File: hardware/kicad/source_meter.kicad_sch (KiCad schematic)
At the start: 39 parts, among them U501 TPS63020DSJ, U502 OPA365AIDBV, U503 LT3080EDD, U504 MCP4921-E/SN, U505 OPA197IDBV

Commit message: feat(hardware)!: draw draft A1 of the schematic around a Pico 2
A Raspberry Pi Pico 2 on two 1x20 sockets replaces the ESP32-S3
development board, the programmable logic device and the buffer
between the two boards (D-39 to D-43 of the specification). The former
interface and range logic sheets become two new ones:

- Controller: the Pico 2, the diodes that join its USB supply and the
  5 V rail of the carrier, resistor arrays in the SPI and acquisition
  lines, a reset button and a console header.
- Side Data: two shift registers that take the range, the status
  signals and the eight logic inputs with every sample.

The DUT connects through a 1x4 pin header and a lever terminal block
in parallel, both GND, VIN, VOUT, GND, and the logic port is a 1x10
header with VCC, GND, D7 to D0: the pin order of the PPK2 (D-44). A
solder jumper selects the supply of the DUT side of the level
translator. A transistor at the driver of the ampere switch holds it
open while VIN is above 5.5 V.

Reference designators are numbered as the annotation tool of KiCad
does by default (D-45). The numbering touches every sheet, so these
changes come in one commit. The symbol and the socket footprint of
the ESP32-S3 board leave the project library; the Pico 2 uses the
symbol and the footprint of the KiCad library.

The electrical rules check reports no errors and no warnings. The
parts stay candidates, and no program for the PIO blocks exists yet.

BREAKING CHANGE: the pins of the controller follow the new pin map of
section 5 of the specification.
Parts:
- R15: renamed from R501; value 470R -> 1k
- renumbered C501 to C24, C513 to C25, C502 to C26, C514 to C27, C503 to C28, C516 to C29, C517 to C30, C507 to C31, C504 to C32, C515 to C33, C505 to C34, C506 to C35, C508 to C36, C509 to C37, C510 to C38, C511 to C39, C512 to C40, FB501 to FB1, L501 to L2, R510 to R16, R511 to R17, R506 to R18, R512 to R19, R502 to R20, R505 to R21, R503 to R22, R504 to R23, R507 to R24, R508 to R25, R509 to R26, TP501 to TP11, TP503 to TP12, TP502 to TP13, U502 to U10, U505 to U11, U503 to U12, U504 to U8, U501 to U9
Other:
- note added: "V_PRE follows the set-point: PRE_FB = 0.2 x (V_PRE - SET_DRV) + 0.41 V and U9 holds it at 0.5 V, so V_PRE = SET_DRV + 0.45 V to 0.49 V (1.26 V at 0.8 V, 5.49 V at 5.0 V). SET_DRV = 2.1 x DAC: 0 V to 5.25 V in 1.28 mV steps. Firmware keeps it between 0.75 V and 5.0 V. U12: IN from V_PRE, VCONTROL from +13V5, minimum load R26 to -4V_A. U9 runs in forced PWM (PS/SYNC high), 2.4 MHz."
- note removed: "V_PRE follows the set-point: PRE_FB = 0.2 x (V_PRE - SET_DRV) + 0.41 V and U501 holds it at 0.5 V, so V_PRE = SET_DRV + 0.45 V to 0.49 V (1.26 V at 0.8 V, 5.49 V at 5.0 V). SET_DRV = 2.1 x DAC: 0 V to 5.25 V in 1.28 mV steps. Firmware keeps it between 0.75 V and 5.0 V. U503: IN from V_PRE, VCONTROL from +13V5, minimum load R509 to -4V_A. U501 runs in forced PWM (PS/SYNC high), 2.4 MHz."

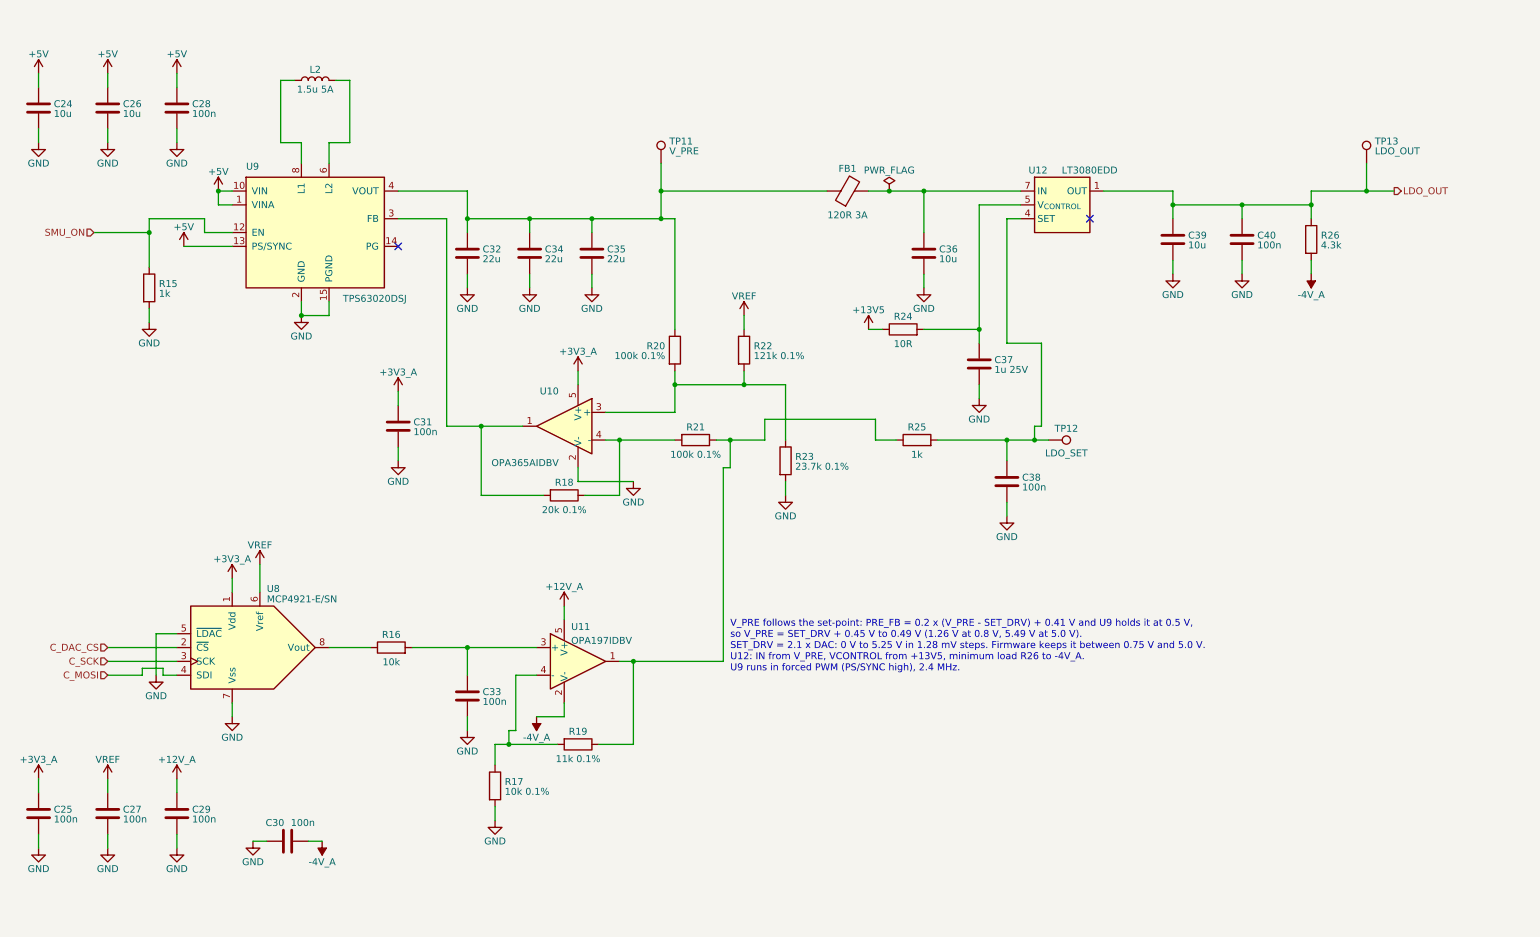
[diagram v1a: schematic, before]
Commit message: feat(hardware): draw draft A2 of the schematic
428 parts on 15 A4 pages, 14 sheets below the root sheet (D-83). Two
sheets are new: Logic Supplies, with the supervisor of the 5 V rail and
the two 3.3 V regulators, and Rail Monitor, with the comparators behind
PWR_GOOD.

The drawings follow the specification of draft A2: a current limiter
on each supply input and a priority multiplexer, a pre-regulator that
tracks the output of the linear regulator, a VIN path that withstands
-20 V to +20 V with its switch open, two diode-connected MOSFETs as
ladder clamp, thin-film and four-terminal shunts, ESD arrays at the CC
pins and at the VCC pin of the logic port. The reference designators
are numbered as KiCad numbers them (D-45), so they are not those of
draft A1.

The project library gains the symbol of the input multiplexer and two
footprints: the lever terminal block with pads of 1.9 mm x 2.3 mm and
the controller module without its antenna keep-out (D-85).

The electrical rules check reports no errors and no warnings. The
parts are candidates, and nothing is built or measured.
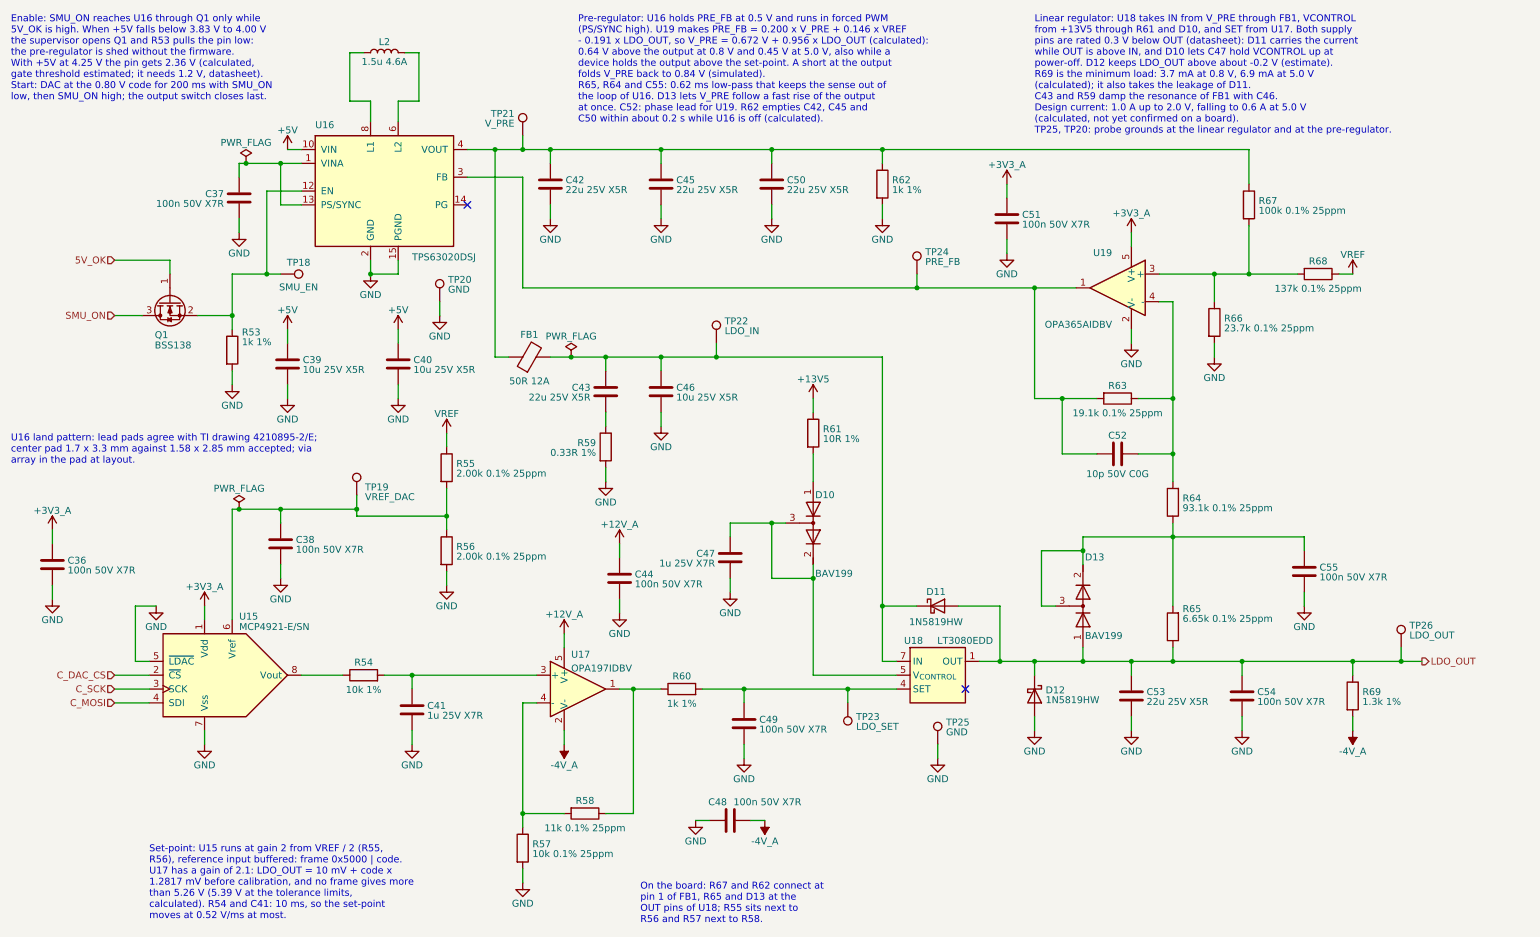
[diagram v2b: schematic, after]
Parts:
- added C43: 22u 25V X5R, Capacitor_SMD:C_1206_3216Metric, symbol Device:C
- added C52: 10p 50V C0G, Capacitor_SMD:C_0603_1608Metric, symbol Device:C
- added C55: 100n 50V X7R, Capacitor_SMD:C_0603_1608Metric, symbol Device:C
- added D10, D13: BAV199, Package_TO_SOT_SMD:SOT-23, symbol Device:D_Dual_Series_AKC
- added D11, D12: 1N5819HW, Diode_SMD:D_SOD-123, symbol Device:D_Schottky
- added Q1: BSS138, Package_TO_SOT_SMD:SOT-23, symbol Transistor_FET:BSS138
- added R55, R56: 2.00k 0.1% 25ppm, Resistor_SMD:R_0603_1608Metric, symbol Device:R
- added R59: 0.33R 1%, Resistor_SMD:R_0805_2012Metric, symbol Device:R
- added R62: 1k 1%, Resistor_SMD:R_0603_1608Metric, symbol Device:R
- added R65: 6.65k 0.1% 25ppm, Resistor_SMD:R_0603_1608Metric, symbol Device:R
- added TP18: SMU_EN, TestPoint:TestPoint_Pad_D1.5mm, symbol Connector:TestPoint
- added TP19: VREF_DAC, TestPoint:TestPoint_Pad_D1.5mm, symbol Connector:TestPoint
- added TP20, TP25: GND, TestPoint:TestPoint_Pad_2.0x2.0mm, symbol Connector:TestPoint
- added TP22: LDO_IN, TestPoint:TestPoint_Pad_D1.5mm, symbol Connector:TestPoint
- added TP24: PRE_FB, TestPoint:TestPoint_Pad_D1.5mm, symbol Connector:TestPoint
- C36: renamed from C25; value 100n -> 100n 50V X7R; MPN (none) -> C0603C104K5RACTU; Manufacturer (none) -> KEMET
- C37: renamed from C28; value 100n -> 100n 50V X7R; MPN (none) -> C0603C104K5RACTU; Manufacturer (none) -> KEMET
- C38: renamed from C27; value 100n -> 100n 50V X7R; MPN (none) -> C0603C104K5RACTU; Manufacturer (none) -> KEMET
- C39: renamed from C24; value 10u -> 10u 25V X5R; MPN (none) -> CL21A106KAYNNNE; Manufacturer (none) -> Samsung Electro-Mechanics
- C40: renamed from C26; value 10u -> 10u 25V X5R; MPN (none) -> CL21A106KAYNNNE; Manufacturer (none) -> Samsung Electro-Mechanics
- C41: renamed from C33; value 100n -> 1u 25V X7R; MPN (none) -> C0603C105K3RACTU; Manufacturer (none) -> KEMET
- C42: renamed from C32; value 22u -> 22u 25V X5R; footprint Capacitor_SMD:C_0805_2012Metric -> Capacitor_SMD:C_1206_3216Metric; MPN (none) -> CL31A226KAHNNNE; Manufacturer (none) -> Samsung Electro-Mechanics
- C44: renamed from C29; value 100n -> 100n 50V X7R; MPN (none) -> C0603C104K5RACTU; Manufacturer (none) -> KEMET
- C45: renamed from C34; value 22u -> 22u 25V X5R; footprint Capacitor_SMD:C_0805_2012Metric -> Capacitor_SMD:C_1206_3216Metric; MPN (none) -> CL31A226KAHNNNE; Manufacturer (none) -> Samsung Electro-Mechanics
- C46: renamed from C36; value 10u -> 10u 25V X5R; MPN (none) -> CL21A106KAYNNNE; Manufacturer (none) -> Samsung Electro-Mechanics
- C47: renamed from C37; value 1u 25V -> 1u 25V X7R; MPN (none) -> C0603C105K3RACTU; Manufacturer (none) -> KEMET
- C48: renamed from C30; value 100n -> 100n 50V X7R; MPN (none) -> C0603C104K5RACTU; Manufacturer (none) -> KEMET
- C49: renamed from C38; value 100n -> 100n 50V X7R; MPN (none) -> C0603C104K5RACTU; Manufacturer (none) -> KEMET
- C50: renamed from C35; value 22u -> 22u 25V X5R; footprint Capacitor_SMD:C_0805_2012Metric -> Capacitor_SMD:C_1206_3216Metric; MPN (none) -> CL31A226KAHNNNE; Manufacturer (none) -> Samsung Electro-Mechanics
- C51: renamed from C31; value 100n -> 100n 50V X7R; MPN (none) -> C0603C104K5RACTU; Manufacturer (none) -> KEMET
- C53: renamed from C39; value 10u -> 22u 25V X5R; footprint Capacitor_SMD:C_0805_2012Metric -> Capacitor_SMD:C_1206_3216Metric; MPN (none) -> CL31A226KAHNNNE; Manufacturer (none) -> Samsung Electro-Mechanics
- C54: renamed from C40; value 100n -> 100n 50V X7R; MPN (none) -> C0603C104K5RACTU; Manufacturer (none) -> KEMET
- FB1: value 120R 3A -> 50R 12A; MPN BLM31PG121SN1L -> BLM31SN500SN1L; Manufacturer (none) -> Murata
- L2: value 1.5u 5A -> 1.5u 4.6A; MPN XFL4020-152ME -> XFL4020-152MEC; Manufacturer (none) -> Coilcraft
- R53: renamed from R15; value 1k -> 1k 1%; MPN (none) -> CRCW06031K00FKEA; Manufacturer (none) -> Vishay
- R54: renamed from R16; value 10k -> 10k 1%; MPN (none) -> CRCW060310K0FKEA; Manufacturer (none) -> Vishay
- R57: renamed from R17; value 10k 0.1% -> 10k 0.1% 25ppm; MPN (none) -> TNPW060310K0BEEA; Manufacturer (none) -> Vishay
- R58: renamed from R19; value 11k 0.1% -> 11k 0.1% 25ppm; MPN (none) -> TNPW060311K0BEEA; Manufacturer (none) -> Vishay
- R60: renamed from R25; value 1k -> 1k 1%; MPN (none) -> CRCW06031K00FKEA; Manufacturer (none) -> Vishay
- R61: renamed from R24; value 10R -> 10R 1%; MPN (none) -> CRCW060310R0FKEA; Manufacturer (none) -> Vishay
- R63: renamed from R18; value 20k 0.1% -> 19.1k 0.1% 25ppm; MPN (none) -> TNPW060319K1BEEA; Manufacturer (none) -> Vishay
- R64: renamed from R21; value 100k 0.1% -> 93.1k 0.1% 25ppm; MPN (none) -> TNPW060393K1BEEA; Manufacturer (none) -> Vishay
- R66: renamed from R23; value 23.7k 0.1% -> 23.7k 0.1% 25ppm; MPN (none) -> TNPW060323K7BEEA; Manufacturer (none) -> Vishay
- R67: renamed from R20; value 100k 0.1% -> 100k 0.1% 25ppm; MPN (none) -> TNPW0603100KBEEA; Manufacturer (none) -> Vishay
- R68: renamed from R22; value 121k 0.1% -> 137k 0.1% 25ppm; MPN (none) -> ERA-3AEB1373V; Manufacturer (none) -> Panasonic
- R69: renamed from R26; value 4.3k -> 1.3k 1%; footprint Resistor_SMD:R_0603_1608Metric -> Resistor_SMD:R_0805_2012Metric; MPN (none) -> CRCW08051K30FKEA; Manufacturer (none) -> Vishay
- TP21: renamed from TP11; now left out of the parts list
- TP23: renamed from TP12; now left out of the parts list
- TP26: renamed from TP13; now left out of the parts list
- U15: renamed from U8; MPN (none) -> MCP4921-E/SN; Manufacturer (none) -> Microchip
- U16: renamed from U9; MPN (none) -> TPS63020DSJR; Manufacturer (none) -> Texas Instruments; Note Land pattern to be drawn from the TI package drawing -> Lead pads agree with TI drawing 4210895-2/E; center pad 1.7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
- U17: renamed from U11; MPN (none) -> OPA197IDBVR; Manufacturer (none) -> Texas Instruments
- U18: renamed from U12; MPN (none) -> LT3080EDD#PBF; Manufacturer (none) -> Analog Devices
- U19: renamed from U10; MPN (none) -> OPA365AIDBVR; Manufacturer (none) -> Texas Instruments
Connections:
- net +5V: no longer C37.1, U16.1 (VINA), U16.13 (PS/SYNC)
- net GND: now also C55.2, D12.2 (A), R56.2, R59.2, R62.2, TP20.1, TP25.1
- net LDO_OUT: now also D11.2 (A), D12.1 (K), D13.1 (A), R65.1
- net SMU_ON: now also Q1.3 (D); no longer R53.1, U16.12 (EN)
- net VREF: now also R55.1; no longer C38.1, U15.6 (Vref)
- net at C42.1, C45.1, C50.1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: now also R62.1
- net at C46.1, FB1.2, U18.7 (IN)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: now also C43.1, D11.1 (K), TP22.1
- net at R58.1, R60.1, U17.1: no longer R64.1
- net at R63.1, R64.2, U19.4 (-): now also C52.1
- net at R63.2, U16.3 (FB), U19.1: now also C52.2, TP24.1
- net at C47.1, U18.5 (V_{CONTROL}): now also D10.2 (K), D10.3 (common); no longer R61.2
- new net: C38.1, R55.2, R56.1, TP19.1, U15.6 (Vref)
- new net: Q1.2 (S), R53.1, TP18.1, U16.12 (EN)
- new net: C37.1, U16.1 (VINA), U16.13 (PS/SYNC)
- new net: C55.1, D13.2 (K), D13.3 (common), R64.1, R65.2
- new net: D10.1 (A), R61.2
- new net: C43.2, R59.1
- new net 5V_OK: Q1.1 (G)
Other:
- note added: "Enable: SMU_ON reaches U16 through Q1 only while 5V_OK is high. When +5V falls below 3.83 V to 4.00 V the supervisor opens Q1 and R53 pulls the pin low: the pre-regulator is shed without the firmware. With +5V at 4.25 V the pin gets 2.36 V (calculated, gate threshold estimated; it needs 1.2 V, datasheet). Start: DAC at the 0.80 V code for 200 ms with SMU_ON low, then SMU_ON high; the output switc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"
- note added: "Linear regulator: U18 takes IN from V_PRE through FB1, VCONTROL from +13V5 through R61 and D10, and SET from U17. Both supply pins are rated 0.3 V below OUT (datasheet): D11 carries the current while OUT is above IN, and D10 lets C47 hold VCONTROL up at power-off. D12 keeps LDO_OUT above about -0.2 V (estimate). R69 is the minimum load: 3.7 mA at 0.8 V, 6.9 mA at 5.0 V (calculated); it also takes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"
- note added: "On the board: R67 and R62 connect at pin 1 of FB1, R65 and D13 at the OUT pins of U18; R55 sits next to R56 and R57 next to R58."
- note added: "Pre-regulator: U16 holds PRE_FB at 0.5 V and runs in forced PWM (PS/SYNC high). U19 makes PRE_FB = 0.200 x V_PRE + 0.146 x VREF - 0.191 x LDO_OUT, so V_PRE = 0.672 V + 0.956 x LDO_OUT (calculated): 0.64 V above the output at 0.8 V and 0.45 V at 5.0 V, also while a device holds the output above the set-point. A short at the output folds V_PRE back to 0.84 V (simulated). R65, R64 and C55: 0.62 ms l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"
- note added: "Set-point: U15 runs at gain 2 from VREF / 2 (R55, R56), reference input buffered: frame 0x5000 | code. U17 has a gain of 2.1: LDO_OUT = 10 mV + code x 1.2817 mV before calibration, and no frame gives more than 5.26 V (5.39 V at the tolerance limits, calculated). R54 and C41: 10 ms, so the set-point moves at 0.52 V/ms at most."
- note added: "U16 land pattern: lead pads agree with TI drawing 4210895-2/E; center pad 1.7 x 3.3 mm against 1.58 x 2.85 mm accepted; via array in the pad at layout."
- note removed: "V_PRE follows the set-point: PRE_FB = 0.2 x (V_PRE - SET_DRV) + 0.41 V and U9 holds it at 0.5 V, so V_PRE = SET_DRV + 0.45 V to 0.49 V (1.26 V at 0.8 V, 5.49 V at 5.0 V). SET_DRV = 2.1 x DAC: 0 V to 5.25 V in 1.28 mV steps. Firmware keeps it between 0.75 V and 5.0 V. U12: IN from V_PRE, VCONTROL from +13V5, minimum load R26 to -4V_A. U9 runs in forced PWM (PS/SYNC high), 2.4 MHz."
- moved on the sheet: C36, C37, C38, C39, C40, C41, C42, C44, C45, C46, C47, C48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
